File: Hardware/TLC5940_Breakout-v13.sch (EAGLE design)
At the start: 51 parts, among them U1 TLC5940-RHB, U2 V_REG_MIC52055V

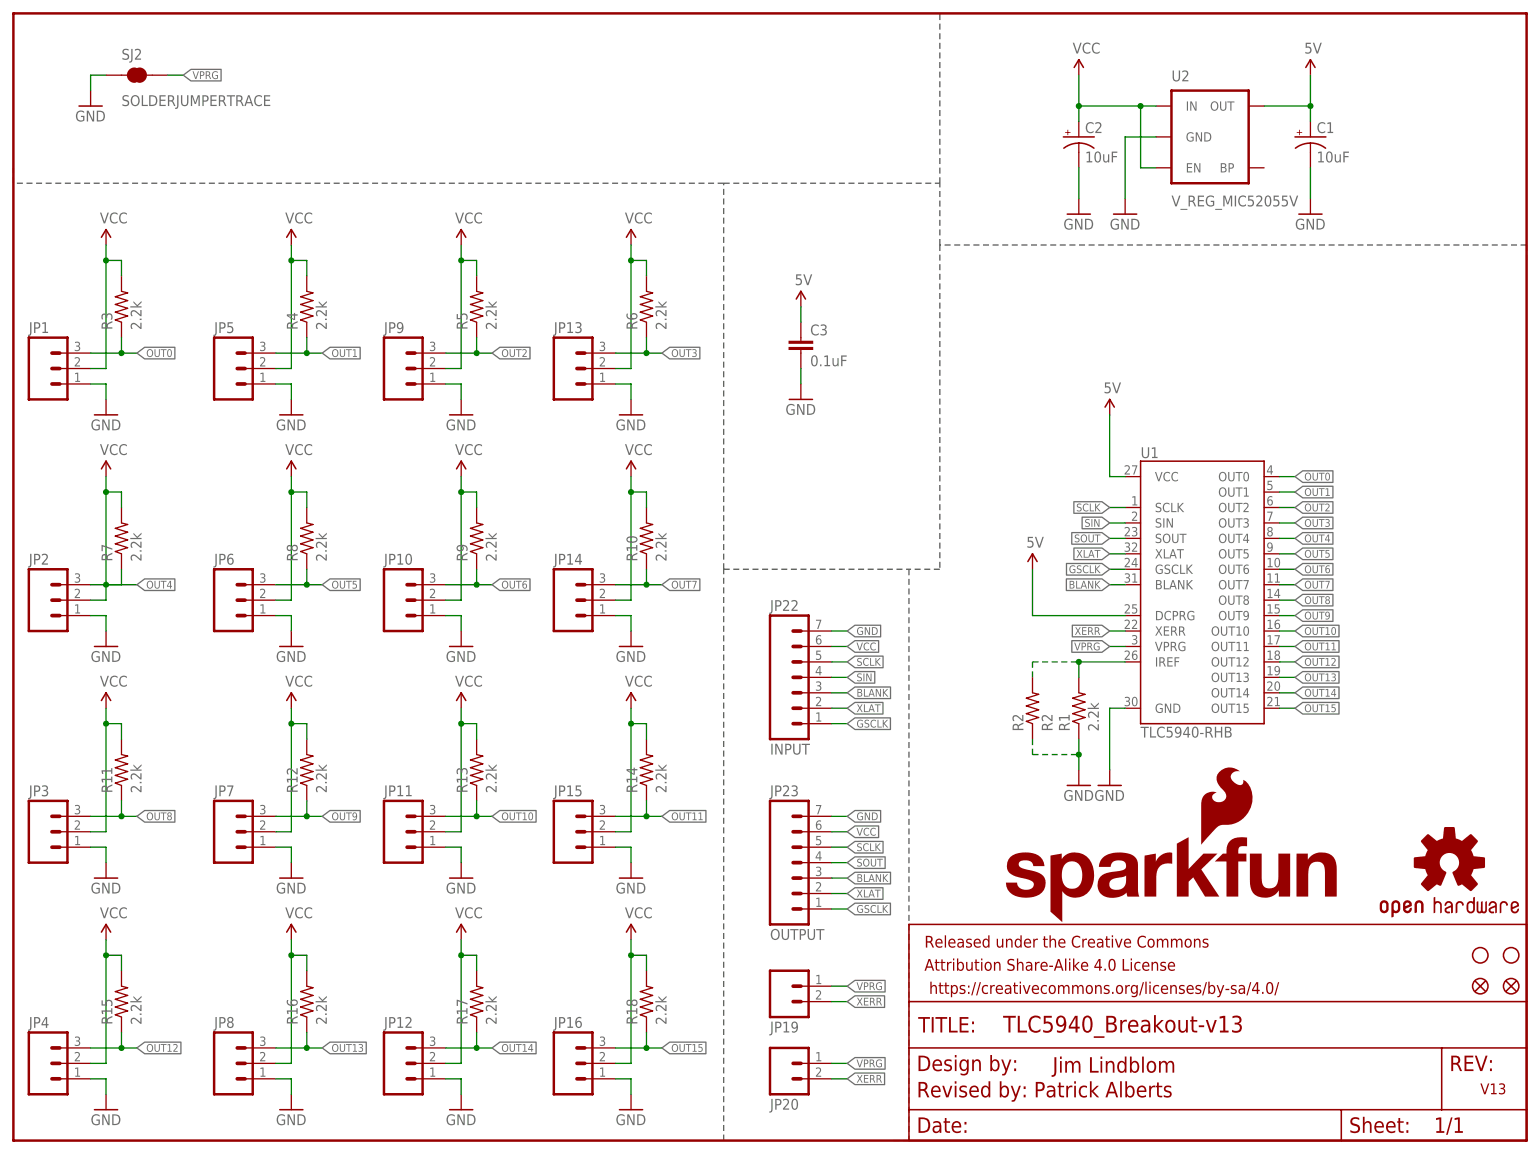
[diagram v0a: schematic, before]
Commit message: Fixed sch issues, updated to 0603, minor re routes.
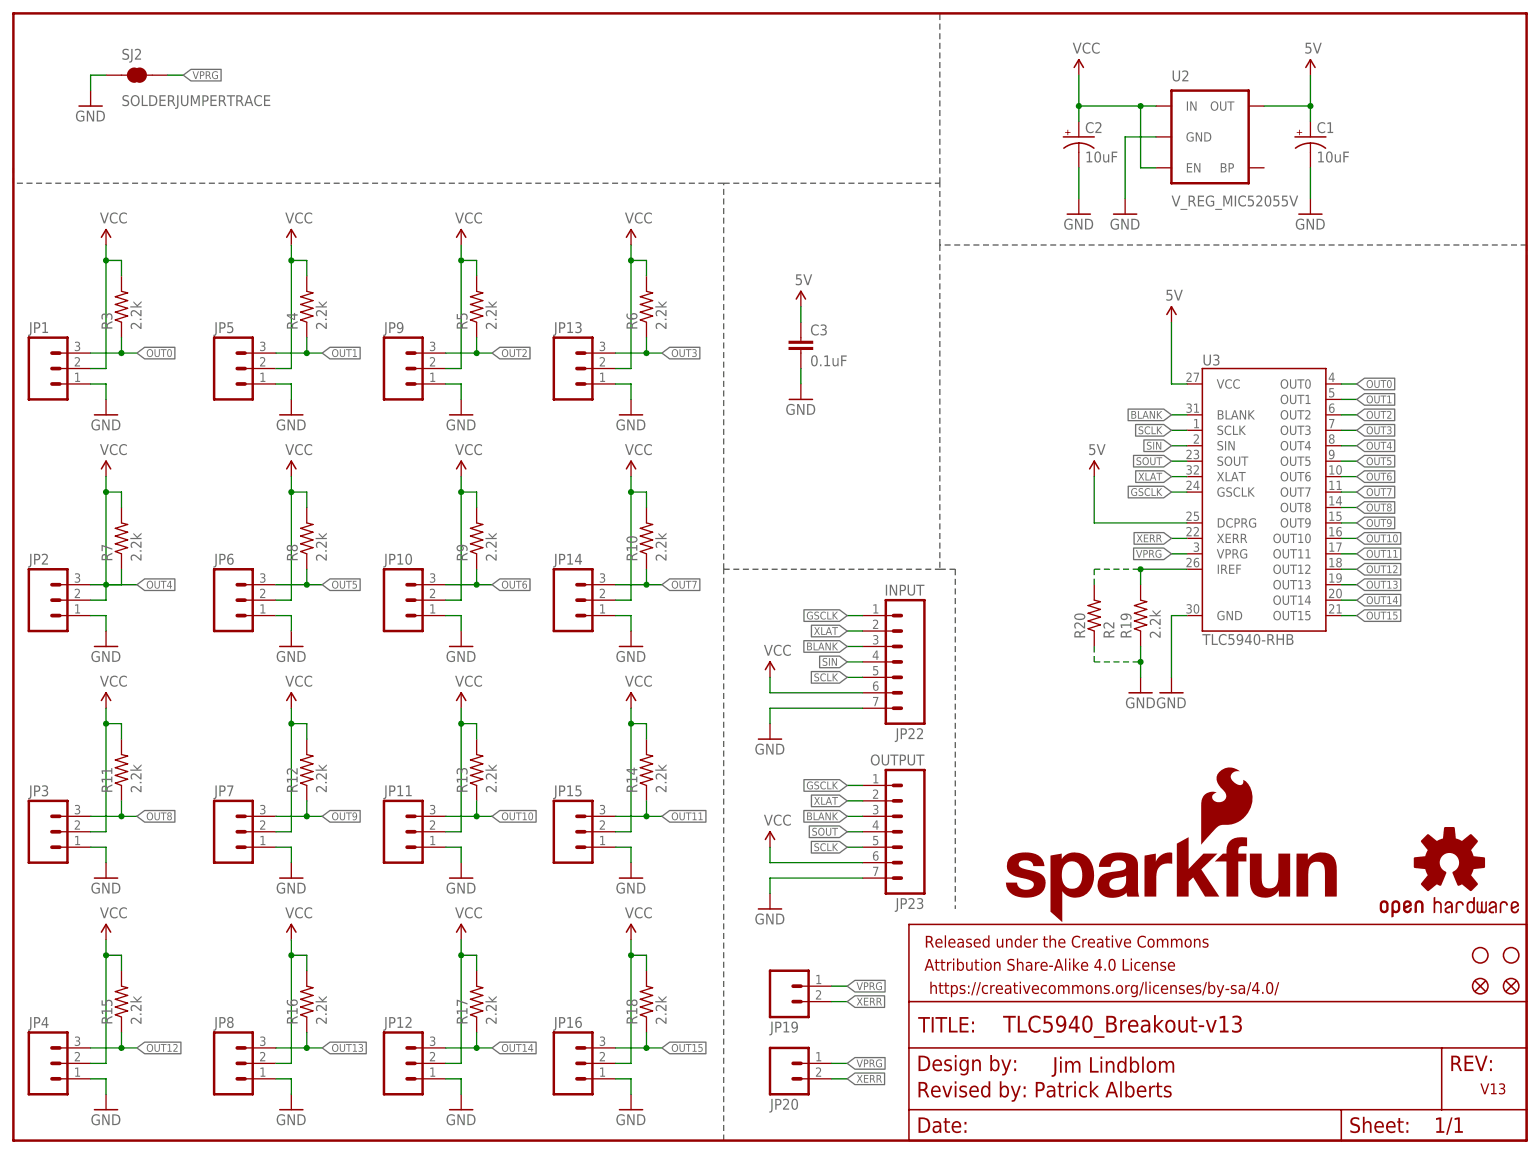
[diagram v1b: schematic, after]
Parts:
- removed R1: 2.2k, SparkFun-Resistors:2.2KOHM-1/10W-1%(0603)
- removed R2: R2, SparkFun-Resistors:RESISTORKIT
- removed U1: TLC5940-RHB, SparkFun:TLC5940-RHB
- added R19: 2.2k, SparkFun-Resistors:2.2KOHM-1/10W-1%(0603)
- added R20: R2, SparkFun-Resistors:RESISTORKIT
- added U3: TLC5940-RHB, SparkFun-DigitalIC:TLC5940-RHB
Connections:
- removed net N$8: R1.2, R2.2, U1.IREF
- new net N$1: R19.2, R20.2, U3.IREF
- net 5V: now also U3.DCPRG, U3.VCC; no longer U1.DCPRG, U1.VCC
- net BLANK: now also U3.BLANK; no longer U1.BLANK
- net GND: now also R19.1, R20.1, U3.GND; no longer R1.1, R2.1, U1.GND
- net GSCLK: now also U3.GSCLK; no longer U1.GSCLK
- net OUT0: now also U3.OUT0; no longer U1.OUT0
- net OUT1: now also U3.OUT1; no longer U1.OUT1
- net OUT10: now also U3.OUT10; no longer U1.OUT10
- net OUT11: now also U3.OUT11; no longer U1.OUT11
- net OUT12: now also U3.OUT12; no longer U1.OUT12
- net OUT13: now also U3.OUT13; no longer U1.OUT13
- net OUT14: now also U3.OUT14; no longer U1.OUT14
- net OUT15: now also U3.OUT15; no longer U1.OUT15
- net OUT2: now also U3.OUT2; no longer U1.OUT2
- net OUT3: now also U3.OUT3; no longer U1.OUT3
- net OUT4: now also U3.OUT4; no longer U1.OUT4
- net OUT5: now also U3.OUT5; no longer U1.OUT5
- net OUT6: now also U3.OUT6; no longer U1.OUT6
- net OUT7: now also U3.OUT7; no longer U1.OUT7
- net OUT8: now also U3.OUT8; no longer U1.OUT8
- net OUT9: now also U3.OUT9; no longer U1.OUT9
- net SCLK: now also U3.SCLK; no longer U1.SCLK
- net SIN: now also U3.SIN; no longer U1.SIN
- net SOUT: now also U3.SOUT; no longer U1.SOUT
- net VPRG: now also U3.VPRG; no longer U1.VPRG
- net XERR: now also U3.XERR; no longer U1.XERR
- net XLAT: now also U3.XLAT; no longer U1.XLAT
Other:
- moved on the sheet: JP22, JP23

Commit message: Fixed QC Checklist issues
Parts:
- removed JP27: FIDUCIAL1X2.5, abes:FIDUCIAL1X2.5
- added JP21: FIDUCIAL1X2, SparkFun:FIDUCIAL1X2
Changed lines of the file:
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@@
 <layer number="56" name="wert" color="7" fill="1" visible="no" active="no"/>
 <layer number="57" name="tCAD" color="7" fill="1" visible="no" active="no"/>
+<layer number="59" name="tCarbon" color="7" fill="1" visible="no" active="no"/>
+<layer number="60" name="bCarbon" color="7" fill="1" visible="no" active="no"/>
 <layer number="90" name="Modules" color="5" fill="1" visible="yes" active="yes"/>
 <layer number="91" name="Nets" color="2" fill="1" visible="yes" active="yes"/>
@@
 <layer number="127" name="_tValues" color="7" fill="1" visible="yes" active="yes"/>
 <layer number="128" name="_bValues" color="7" fill="1" visible="yes" active="yes"/>
+<layer number="129" name="Mask" color="7" fill="1" visible="yes" active="yes"/>
 <layer number="131" name="tAdjust" color="7" fill="1" visible="yes" active="yes"/>
 <layer number="132" name="bAdjust" color="7" fill="1" visible="yes" active="yes"/>
@@
 <layer number="223" name="223bmp" color="24" fill="1" visible="no" active="no"/>
 <layer number="224" name="224bmp" color="25" fill="1" visible="no" active="no"/>
+<layer number="225" name="225bmp" color="7" fill="1" visible="yes" active="yes"/>
+<layer number="226" name="226bmp" color="7" fill="1" visible="yes" active="yes"/>
+<layer number="227" name="227bmp" color="7" fill="1" visible="yes" active="yes"/>
+<layer number="228" name="228bmp" color="7" fill="1" visible="yes" active="yes"/>
+<layer number="229" name="229bmp" color="7" fill="1" visible="yes" active="yes"/>
+<layer number="230" name="230bmp" color="7" fill="1" visible="yes" active="yes"/>
+<layer number="231" name="231bmp" color="7" fill="1" visible="yes" active="yes"/>
 <layer number="248" name="Housing" color="7" fill="1" visible="yes" active="yes"/>
 <layer number="249" name="Edge" color="7" fill="1" visible="yes" active="yes"/>
@@
 <part name="R18" library="SparkFun-Resistors" deviceset="2.2KOHM-1/10W-1%(0603)" device="" value="2.2k"/>
 <part name="JP26" library="SparkFun" deviceset="FIDUCIAL" device="1X2"/>
-<part name="JP27" library="abes" deviceset="FIDUCIAL" device="1X2.5"/>
 <part name="LOGO1" library="SparkFun-Aesthetics" deviceset="OSHW-LOGO" device="S"/>
 <part name="LOGO2" library="SparkFun-Aesthetics" deviceset="SFE_LOGO_NAME_FLAME" device=".2_INCH" value="SFE_LOGO_NAME_FLAME.2_INCH"/>
@@
 <part name="GND2" library="SparkFun" deviceset="GND" device=""/>
 <part name="P+2" library="SparkFun" deviceset="VCC" device=""/>
+<part name="JP21" library="SparkFun" deviceset="FIDUCIAL" device="1X2"/>
 </parts>
 <sheets>
@@
 <instance part="R18" gate="G$1" x="104.14" y="22.86" rot="R90"/>
 <instance part="JP26" gate="G$1" x="241.3" y="25.4"/>
-<instance part="JP27" gate="G$1" x="246.38" y="25.4"/>
 <instance part="LOGO1" gate="G$1" x="236.22" y="45.72"/>
 <instance part="LOGO2" gate="G$1" x="162.56" y="35.56"/>
@@
 <instance part="GND2" gate="1" x="124.46" y="38.1"/>
 <instance part="P+2" gate="1" x="124.46" y="48.26"/>
+<instance part="JP21" gate="G$1" x="246.38" y="25.4"/>
 </instances>
 <busses>
